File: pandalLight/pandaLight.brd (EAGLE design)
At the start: 160 x 100 mm, 115 parts, among them J1 PJ-037A, U13 TPD12S016PWR, U15 PMOD-2X6, U16 PMOD-2X6, U17 PLR135-T10, U18 PLT133-T10W, U20 TP10SQ, U21 TP10SQ, U22 PAN1322, U23 6SLX9TQG144, U3 TPD4S014SON, U4 FT2232HL, U5 93LC46BT-I/OT, U6 51, U7 51, U8 TPD12S016PWR, X1 USBUB-S, X2 HDMI_RECEPTICAL_A, X4 HDMI_RECEPTICAL_A, Y1 403, Y2 20Mhz

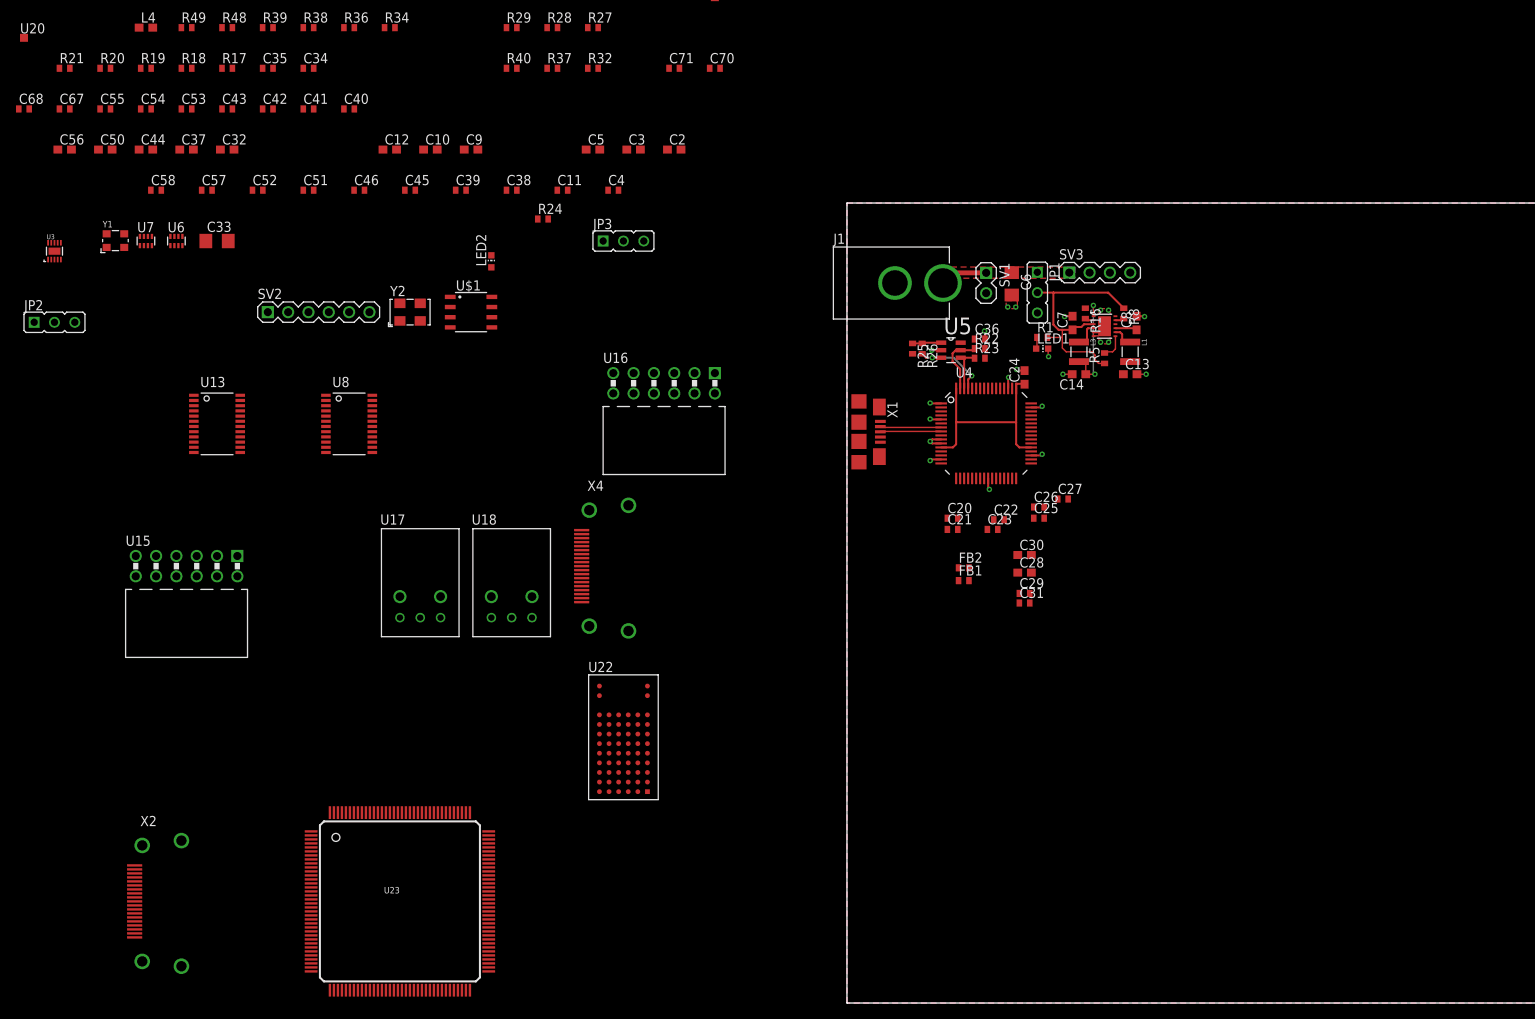
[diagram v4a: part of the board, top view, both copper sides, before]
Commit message: Removed the USB companion chip; Routed USB part
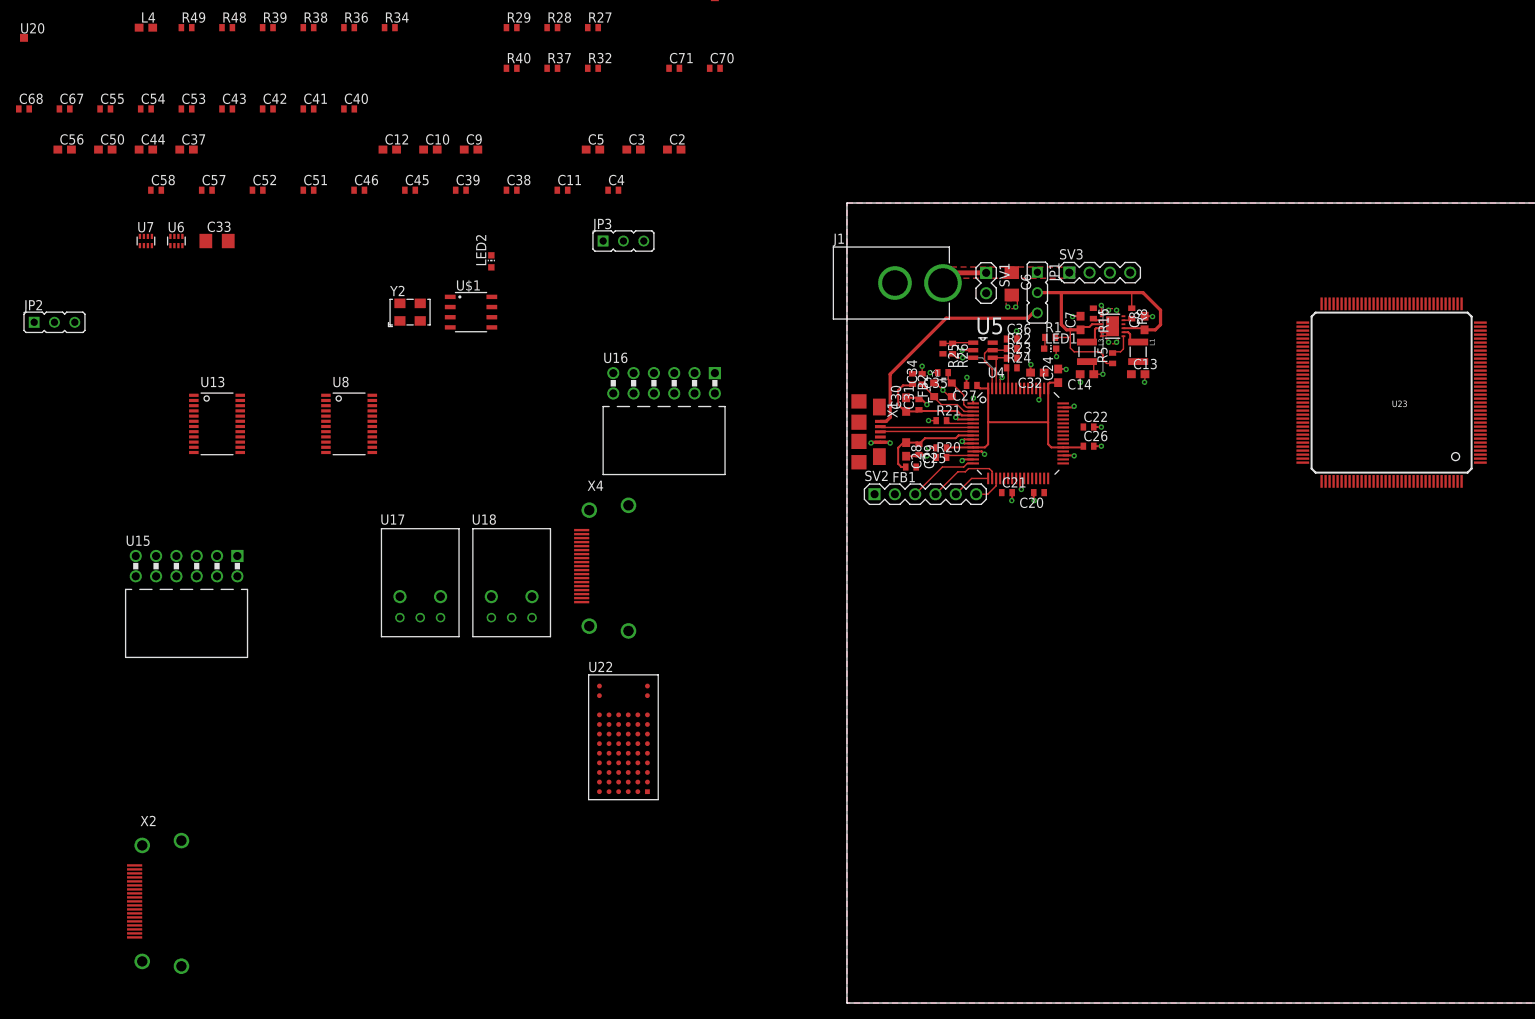
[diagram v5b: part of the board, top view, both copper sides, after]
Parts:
- removed C23: 0.1u, pandaLight:0402
- removed R17, R19: 10k, pandaLight:0402
- removed R18: 1k, pandaLight:0402
- removed U3: TPD4S014SON, pandaLight:SON10
- moved U23 139.3 mm to (68.1, 76.3), turned to 180 degrees
- moved R21 118.1 mm to (11.8, 72.8)
- moved R20 115.3 mm to (11.8, 68.2)
- moved Y1 105.1 mm to (12.0, 76.6)
- moved C32 105.0 mm to (23.8, 78.8), turned to 180 degrees
- moved C35 92.6 mm to (12.0, 78.8), turned to 180 degrees
- moved C34 86.0 mm to (9.40, 78.0), turned to 90 degrees
- moved SV2 79.2 mm to (9.80, 63.6)
- moved R24 61.5 mm to (20.6, 79.4)
- moved C31 28.1 mm to (9.00, 74.8), turned to 90 degrees
- moved FB2 24.5 mm to (8.20, 78.0), turned to 270 degrees
- moved C30 23.9 mm to (7.40, 74.8), turned to 90 degrees
- moved C29 22.3 mm to (9.00, 69.2), turned to 270 degrees
- moved C28 21.4 mm to (7.40, 69.2), turned to 270 degrees
- moved C27 18.2 mm to (15.6, 77.2), turned to 180 degrees
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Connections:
- removed net N$45: C33.1, U3.10, U3.9, X1.VBUS
- removed net USB_5V_ACK#: R17.1, R18.1, U3.4
- removed net USB_5V_DISABLE: R19.2, U3.3
- removed net USB_5V_OFF: R18.2
- net +3V3: no longer C23.1, R17.2
- net GND: no longer C23.2, R19.1, U3.8, U3.ETP
- net N$7: no longer U3.6
- net N$8: no longer U3.7
- net USB_VBUS: now also C33.1, X1.VBUS; no longer U3.1, U3.2
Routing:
- net USB_VBUS: track 0.00 -> 28.4 mm
- net GND: track 21.5 -> 44.1 mm, vias 22 -> 38
- net N$28: track 0.00 -> 14.0 mm
- net N$31: track 0.00 -> 13.3 mm
- net +5V: track 34.5 -> 45.2 mm
- net USB_TDO: track 0.00 -> 9.43 mm
- net USB_TCK: track 0.00 -> 8.84 mm
- net N$5: track 0.00 -> 8.01 mm
- net +1V8: track 27.1 -> 34.9 mm
- net N$1: track 0.00 -> 6.13 mm
- net USB_TDI: track 0.00 -> 4.86 mm
- net N$7: track 7.70 -> 11.6 mm
- net N$8: track 7.72 -> 11.6 mm
- net USB_TMS: track 0.00 -> 3.86 mm
- net N$11: track 0.00 -> 3.47 mm
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
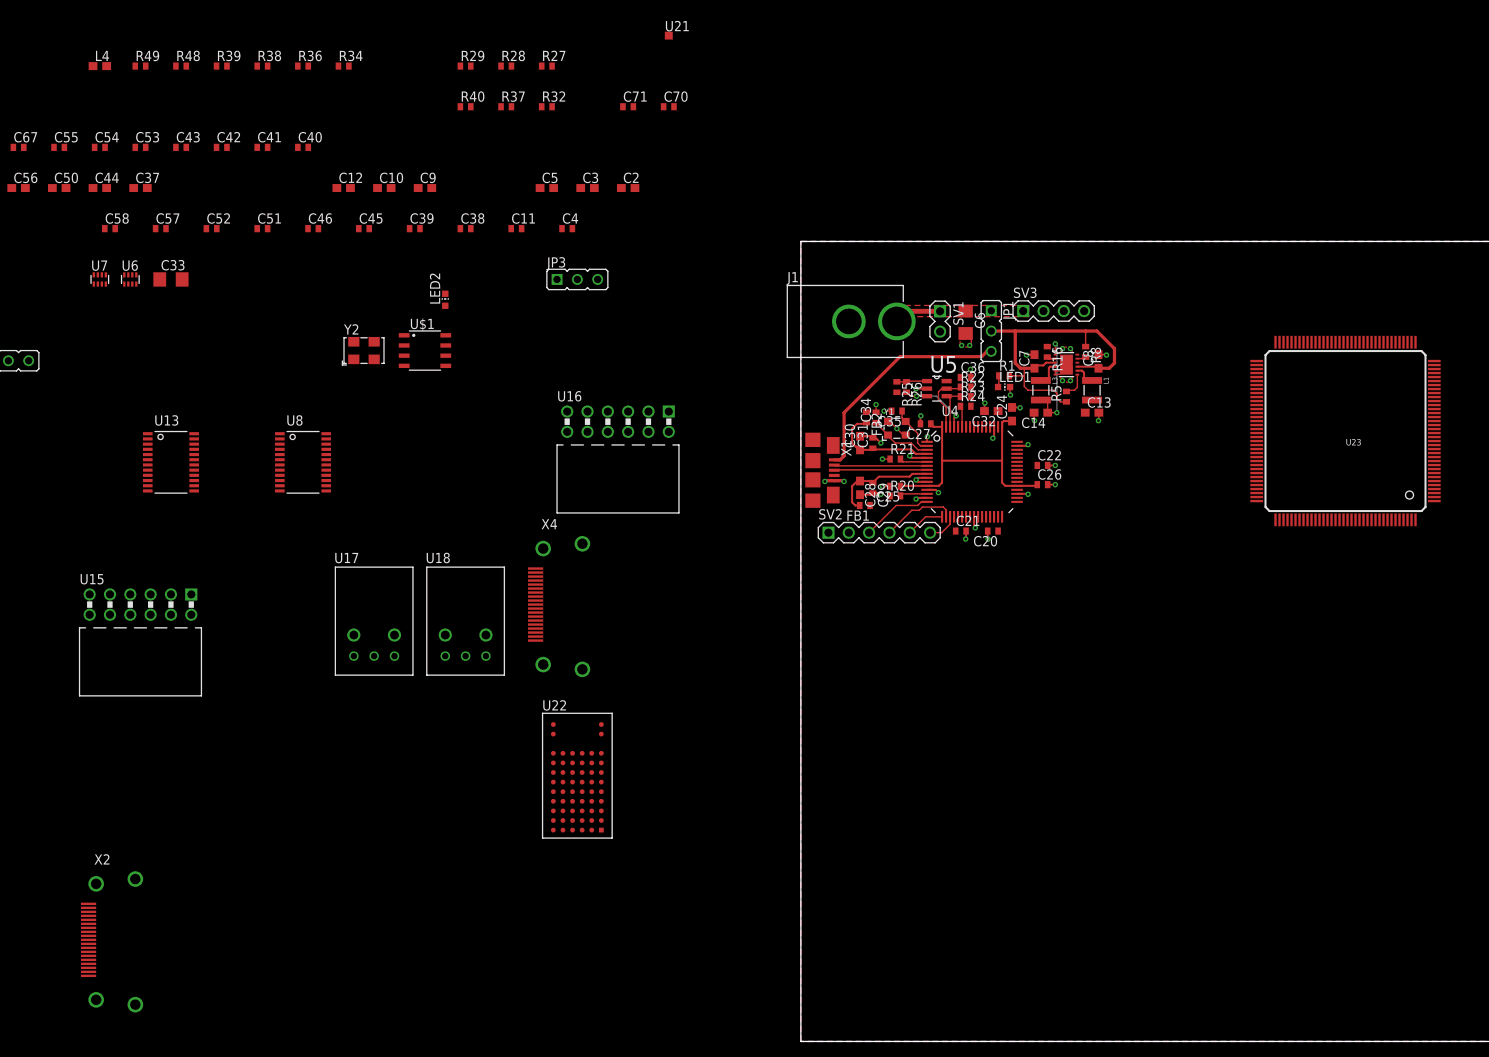
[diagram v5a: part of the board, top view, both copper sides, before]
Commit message: Routed HDMI TX
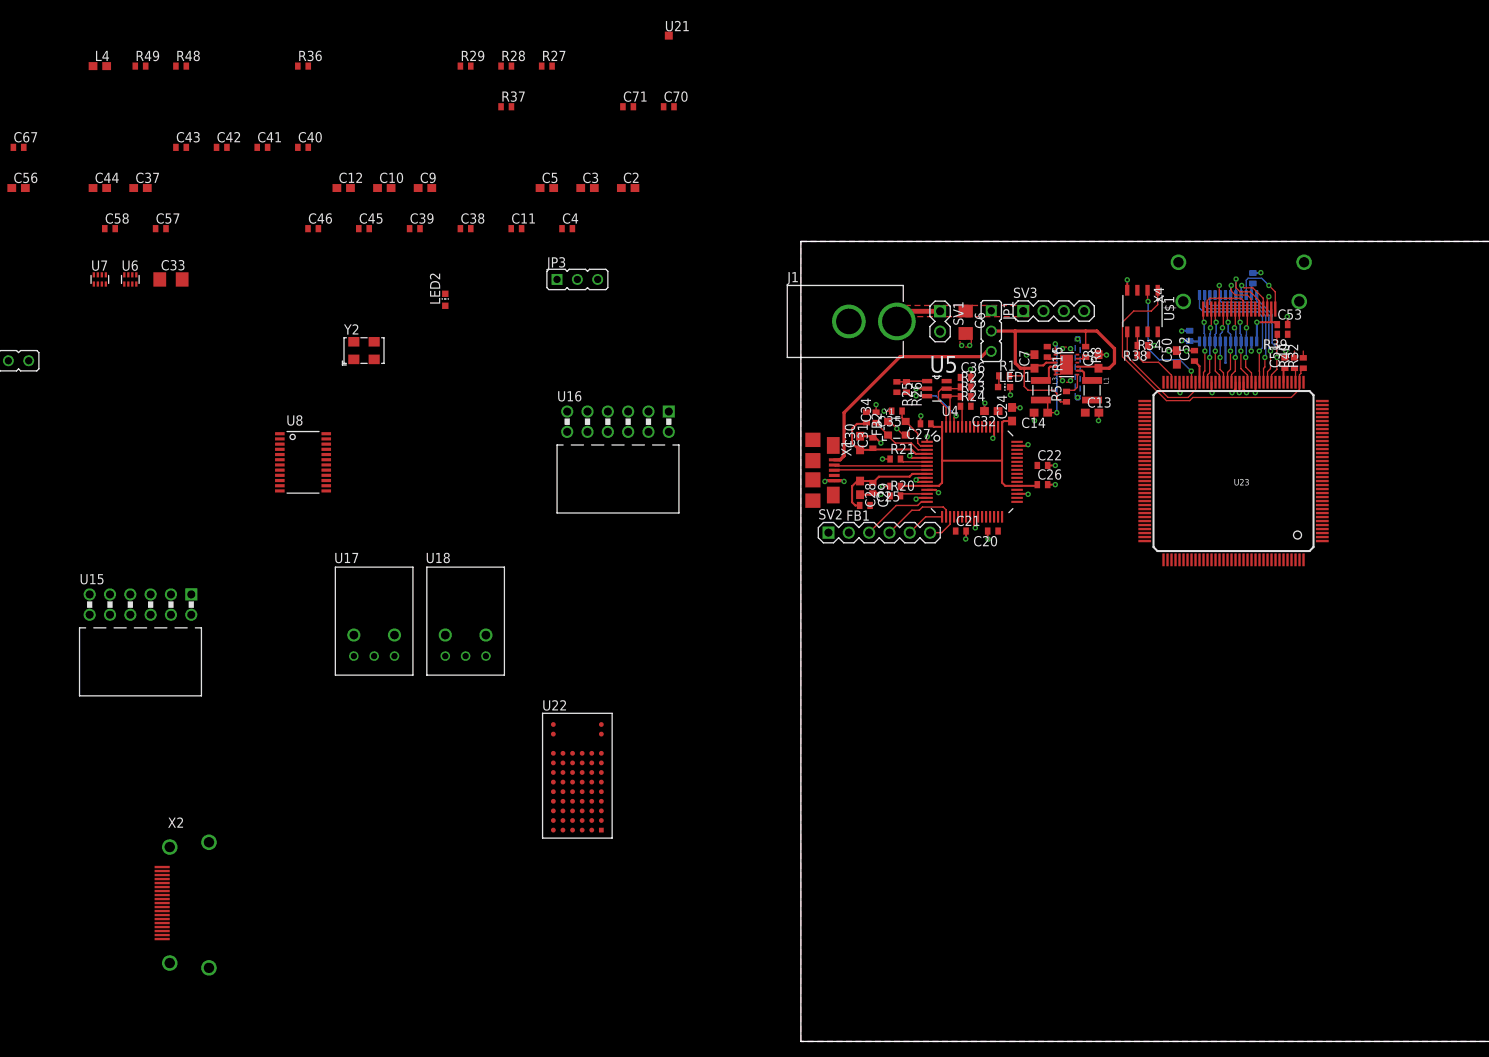
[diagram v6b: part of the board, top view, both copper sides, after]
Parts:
- moved C54 145.1 mm to (56.5, 95.4), flipped to the bottom, turned to 90 degrees
- moved C53 144.5 mm to (60.2, 89.6)
- moved C55 143.3 mm to (48.6, 88.2), flipped to the bottom, turned to 90 degrees
- moved C50 141.3 mm to (47.0, 85.5), turned to 90 degrees
- moved R39 136.8 mm to (60.2, 88.4), turned to 180 degrees
- moved U13 133.4 mm to (53.4, 90.4), flipped to the bottom, turned to 270 degrees
- moved C51 128.9 mm to (60.5, 84.8), turned to 90 degrees
- moved C52 123.9 mm to (49.2, 85.7), turned to 90 degrees
- moved R38 115.4 mm to (42.7, 87.0), turned to 180 degrees
- moved R40 108.5 mm to (61.7, 84.8), turned to 90 degrees
- moved R34 106.2 mm to (42.7, 85.8)
- moved R32 99.8 mm to (62.8, 84.8), turned to 90 degrees
- moved X4 93.4 mm to (54.8, 95.5), turned to 90 degrees
- moved U$1 89.8 mm to (42.7, 91.3), turned to 270 degrees
- moved U23 14.9 mm to (54.1, 71.3)
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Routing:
- net N$41: track 0.00 -> 39.2 mm
- net GND: track 44.1 -> 74.4 mm, vias 38 -> 53
- net HDMI_TX_CTRL_EN: track 0.00 -> 20.7 mm, vias 0 -> 1
- net HDMI_TX_CEC_3V3: track 0.00 -> 18.3 mm, vias 0 -> 1
- net HDMI_TX_SCL_3V3: track 0.00 -> 17.9 mm, vias 0 -> 1
- net HDMI_TX_SDA_3V3: track 0.00 -> 17.7 mm, vias 0 -> 1
- net N$43: track 0.00 -> 15.3 mm, vias 0 -> 2
- net N$40: track 0.00 -> 15.1 mm
- net +3V3: track 0.00 -> 10.0 mm, vias 0 -> 4
- net HDMI_TX_CLK_P: track 0.00 -> 9.60 mm, vias 0 -> 2
- net HDMI_TX_CLK_N: track 0.00 -> 9.54 mm, vias 0 -> 2
- net HDMI_TX_DATA1_N: track 0.00 -> 9.49 mm, vias 0 -> 2
- net HDMI_TX_DATA0_P: track 0.00 -> 9.49 mm, vias 0 -> 2
- net HDMI_TX_DATA0_N: track 0.00 -> 9.49 mm, vias 0 -> 2
- net HDMI_TX_DATA1_P: track 0.00 -> 9.47 mm, vias 0 -> 2
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- added copper zone on layer 16, net +3V3

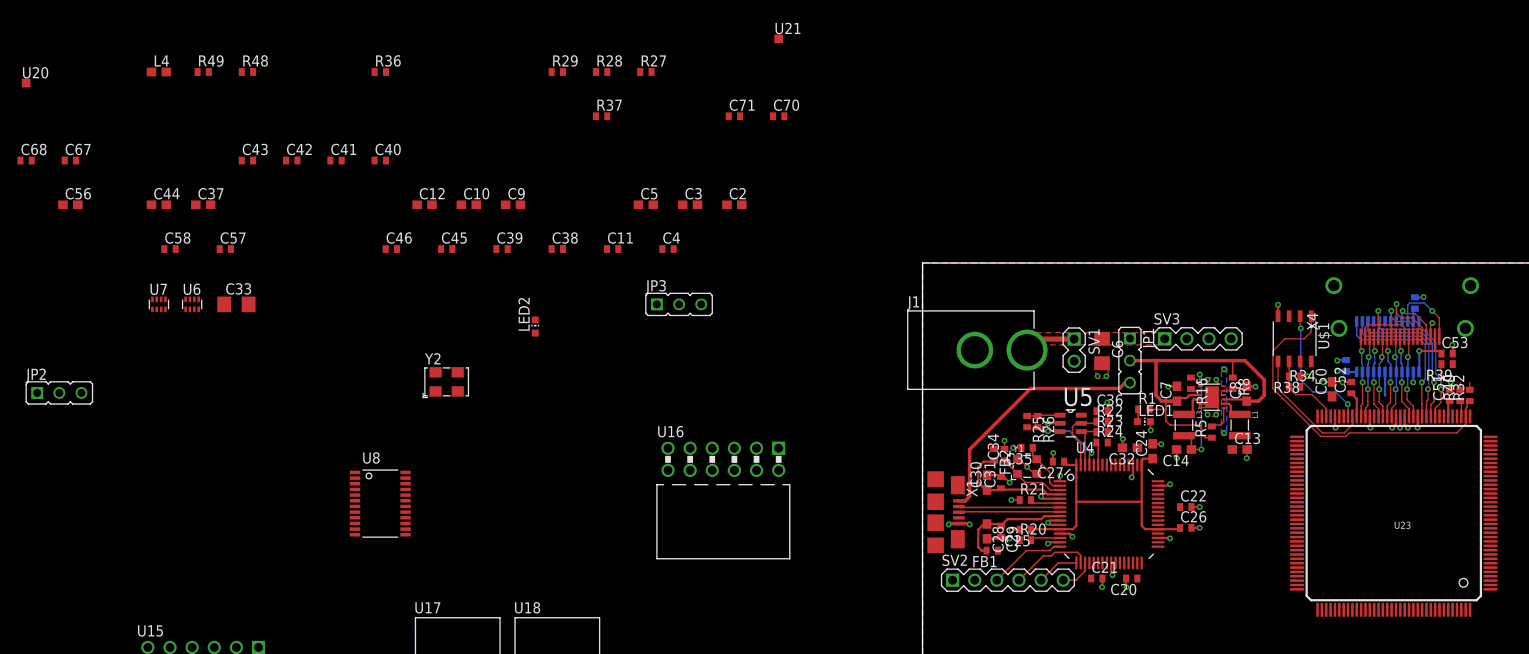
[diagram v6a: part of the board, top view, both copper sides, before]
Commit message: Minor library changes; Searching for CMOS to TTL level shifters for the LED strip outputs
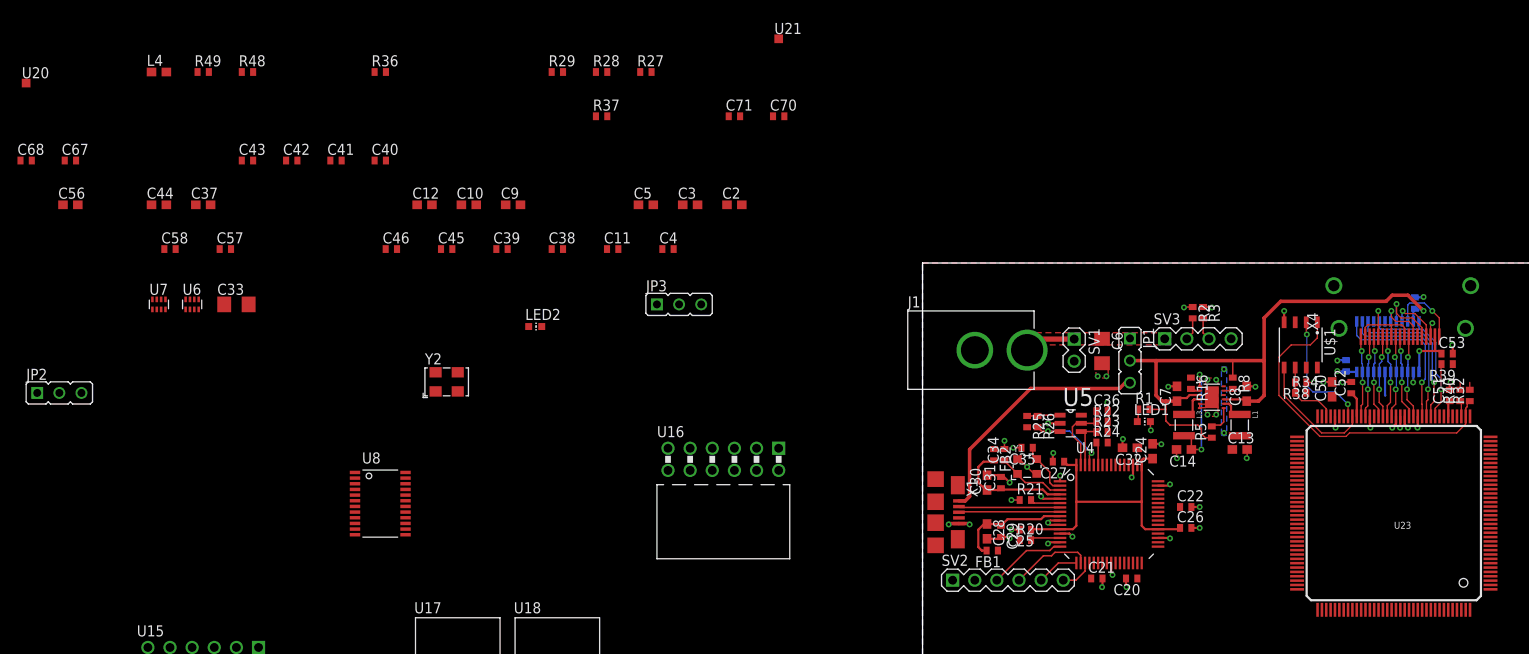
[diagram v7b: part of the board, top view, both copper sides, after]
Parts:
- added R2, R3: 10k, pandaLight:0402
- moved R34 0.99 mm to (43.4, 85.1)
- moved R38 0.99 mm to (43.4, 86.3)
- moved U$1 0.99 mm to (43.4, 90.6)
- turned LED1 to 0 degrees
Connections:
- net GND: now also R2.1, R3.1
- net LEDS_CLK: now also R3.2
- net LEDS_DATA: now also R2.2
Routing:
- net +5V: track 46.7 -> 74.2 mm, vias 0 -> 1
- net LEDS_DATA: track 0.00 -> 2.63 mm
- net LEDS_CLK: track 0.00 -> 2.63 mm
- net GND: track 74.4 -> 76.4 mm, vias 53 -> 55
- net N$43: track 15.3 -> 14.3 mm
- net N$42: track 9.27 -> 8.28 mm
- net N$40: track 15.1 -> 14.2 mm
- net N$41: track 39.2 -> 38.3 mm
